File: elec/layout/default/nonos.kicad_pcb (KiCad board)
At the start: 4 copper layers, 45 x 122 mm, 74 parts, among them CN1 HRSHirose_DF40C_100DS_0_4V51, CN2 HRSHirose_DF40C_100DS_0_4V51, Q1 MOSFET, U1 STUSB4500QTR, U2 _Texas_Instruments_SN74LVC1G0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, U3 _Texas_Instruments_TAS5825MRH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, U4 _HCTL_HC_TYPE_C_24P_VS9_3_5A_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, U5 JST_Sales_America_B02B_XASK_1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, U6 JST_Sales_America_B02B_XASK_1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, U7 _Texas_Instruments_TPS56637RP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

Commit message: Update to newest atopile syntax
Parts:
- C11, C12, C7, C8: footprint lcsc:C0603 -> lcsc:CAP-SMD_L1.6-W0.8-3
- C15: value 4.7µF ±10% 16V X5R -> 100nF ±10% 50V X7R
- C16, C20, C21, C22, C27: value 100nF ±10% 16V X7R -> 100nF ±10% 50V X7R; footprint lcsc:C0402 -> lcsc:C0603
- C17, C18, C19: value 22µF ±20% 25V X5R -> 100nF ±10% 50V X7R; footprint lcsc:C0805 -> lcsc:C0603
- C2, C23, C3, C5, C6: value 1µF ±10% 25V X5R -> 1µF ±10% 10V X5R
- C24, C25, C26: value 4.7µF ±10% 25V X5R -> 100nF ±10% 50V X7R; footprint lcsc:C0805 -> lcsc:C0603
- C28: value 47µF ±20% 6.3V X5R -> 100nF ±10% 50V X7R; footprint lcsc:C0805 -> lcsc:C0603
- D4, D5: footprint lcsc:LED0805-R-RD -> lcsc:LED0402-RD
- R13, R14: value 10kΩ ±1% 62.5mW -> 4.7kΩ ±1% 62.5mW
- R15: value 22kΩ ±1% 62.5mW -> 20kΩ ±1% 62.5mW
- R16: value 8.2kΩ ±1% 62.5mW -> 10kΩ ±1% 62.5mW
- R17: value 68kΩ ±1% 62.5mW -> 75kΩ ±1% 62.5mW
- R19, R20: value 5.1kΩ ±1% 62.5mW -> 1kΩ ±1% 100mW; footprint lcsc:R0402 -> lcsc:R0603
- R2, R3: value 4.7kΩ ±1% 62.5mW -> 10kΩ ±1% 62.5mW
- R8, R9: value 470Ω ±1% 62.5mW -> 470Ω ±1% 100mW; footprint lcsc:R0402 -> lcsc:R0603
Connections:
- net pins[26] renamed processor.hdi_b-pins[26]
- net pins[38] renamed processor.hdi_b-pins[38]
- net processor-pins[44]-1 renamed pins[44]
- net processor-pins[46]-1 renamed pins[46]
- net processor.hdi_b-pins[40] renamed pins[40]
- C11 pad 1: amplifier-net-3 -> amplifier-net-8
- C11 pad 2: amplifier-net-2 -> amplifier-net-9
- C12 pad 1: amplifier-net-7 -> amplifier-net-10
- C12 pad 2: amplifier-net -> amplifier-net-11
- C13 pad 1: net-1 -> net-4
- C14 pad 1: net -> net-5
- C23 pad 1: amplifier-net-6 -> amplifier-net
- C29 pad 1: regulator-net -> regulator-net-3
- C29 pad 2: regulator-net-1 -> regulator-net-2
- C30 pad 1: regulator-net-2 -> regulator-net-4
- C30 pad 2: regulator-net-3 -> regulator-net
- C4 pad 1: pd_controller-net-3 -> pd_controller-net-4
- C5 pad 1: amplifier-net-10 -> amplifier-net-5
- C6 pad 1: amplifier-net-1 -> amplifier-net-6
- C7 pad 1: amplifier-net-11 -> amplifier-net-3
- C7 pad 2: amplifier-net-8 -> amplifier-net-4
- C8 pad 1: amplifier-net-4 -> amplifier-net-7
- C8 pad 2: amplifier-net-5 -> amplifier-net-2
- C9 pad 1: net-3 -> net-1
- CN1 pad 12: processor-signal -> processor-signal-1
- CN1 pad 15: signal-3 -> signal-1
- CN1 pad 17: signal-4 -> signal-2
- CN1 pad 24: processor-signal-2 -> processor-signal-5
- CN1 pad 27: signal-5 -> signal-3
- CN1 pad 28: signal-2 -> net
- CN1 pad 29: signal-1 -> net-3
- CN1 pad 77: processor-pins[46] -> processor-signal-6
- CN1 pad 78: processor-pins[44] -> processor-signal-2
- CN1 pad 80: processor-pins[40] -> processor-signal-4
- CN1 pad 81: processor-signal-1 -> processor-pins[38]
- CN1 pad 82: signal -> signal-4
- CN1 pad 85: processor-signal-6 -> pins[30]
- CN1 pad 86: processor-signal-5 -> processor-signal
- CN1 pad 87: processor-signal-4 -> processor-pins[26]
- D4 pad 1: VCC_3V3 -> processor-net-3
- D4 pad 2: processor-net-3 -> VCC_3V3
- D5 pad 1: VCC_3V3 -> processor-net-1
- D5 pad 2: processor-net-1 -> VCC_3V3
- FPC1 pad 10: signal -> signal-4
- FPC1 pad 7: signal-5 -> signal-3
- FPC1 pad 8: signal-4 -> signal-2
- FPC1 pad 9: signal-3 -> signal-1
- L1 pad 1: amplifier-net-8 -> amplifier-net-4
- L1 pad 2: net-3 -> net-1
- L2 pad 1: amplifier-net-5 -> amplifier-net-2
- L3 pad 1: amplifier-net-2 -> amplifier-net-9
- L3 pad 2: net-1 -> net-4
- L4 pad 1: amplifier-net -> amplifier-net-11
- L4 pad 2: net -> net-5
- L5 pad 2: regulator-net-1 -> regulator-net-2
- Q1 pad 4: pd_controller-net-2 -> pd_controller-net
- R1 pad 2: pd_controller-net-1 -> pd_controller-net-3
- R10 pad 1: amplifier-net-9 -> amplifier-net-1
- R11 pad 1: signal-1 -> net
- R12 pad 1: signal-7 -> signal-5
- R13 pad 1: signal-2 -> SCL
- R14 pad 1: signal-6 -> SDA
- R15 pad 2: regulator-net-2 -> regulator-net-4
- R16 pad 2: regulator-net-3 -> regulator-net
- R17 pad 2: regulator-net-3 -> regulator-net
- R18 pad 2: regulator-net-4 -> regulator-net-1
- R2 pad 1: SCL -> net-3
- R3 pad 1: SDA -> signal
- R4 pad 2: pd_controller-net -> pd_controller-net-2
- R5 pad 1: pd_controller-net-2 -> pd_controller-net
- R6 pad 1: pd_controller-net-2 -> pd_controller-net
- R6 pad 2: pd_controller-net-4 -> pd_controller-net-1
- R7 pad 1: pd_controller-net-2 -> pd_controller-net
- R7 pad 2: pd_controller-net-3 -> pd_controller-net-4
- R8 pad 2: rj45-net-1 -> rj45-net
- R9 pad 2: rj45-net -> rj45-net-1
- RJ1 pad 12: rj45-net-1 -> rj45-net
- RJ1 pad 13: rj45-net -> rj45-net-1
- U1 pad 1: pd_controller.pd_controller-signal-1 -> pd_controller.pd_controller-signal
- U1 pad 16: pd_controller-net-4 -> pd_controller-net-1
- U1 pad 18: pd_controller-net -> pd_controller-net-2
- U1 pad 5: pd_controller.pd_controller-signal -> pd_controller.pd_controller-signal-1
- U1 pad 9: pd_controller-net-1 -> pd_controller-net-3
- U3 pad 1: amplifier-net-4 -> amplifier-net-7
- U3 pad 10: signal-7 -> signal
- U3 pad 11: signal-6 -> signal-5
- U3 pad 17: signal-2 -> net
- U3 pad 18: amplifier-net-1 -> amplifier-net-6
- U3 pad 19: amplifier-net-10 -> amplifier-net-5
- U3 pad 2: amplifier-net-5 -> amplifier-net-2
- U3 pad 23: amplifier-net -> amplifier-net-11
- U3 pad 24: amplifier-net-7 -> amplifier-net-10
- U3 pad 27: amplifier-net-2 -> amplifier-net-9
- U3 pad 28: amplifier-net-3 -> amplifier-net-8
- U3 pad 29: amplifier-net-11 -> amplifier-net-3
- U3 pad 30: amplifier-net-8 -> amplifier-net-4
- U3 pad 7: amplifier-net-6 -> amplifier-net
- U3 pad 8: amplifier-net-9 -> amplifier-net-1
- U3 pad 9: signal-1 -> net-3
- U5 pad 2: net-3 -> net-1
- U6 pad 1: net-1 -> net-4
- U6 pad 2: net -> net-5
- U7 pad 2: regulator-net-3 -> regulator-net
- U7 pad 4: regulator-net-4 -> regulator-net-1
- U7 pad 6: regulator-net-1 -> regulator-net-2
- U7 pad 7: regulator-net -> regulator-net-3
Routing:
- net (no net): track 0.00 -> 3.61 mm
- net signal-7: track 1.91 -> 0.00 mm
- net signal-6: track 1.70 -> 0.00 mm

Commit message: Build full
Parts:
- D2, D3: value (none) -> infV
- D4, D5: value (none) -> 2V; footprint lcsc:LED0402-RD -> lcsc:LED0603-RD
- L1, L2, L3, L4: value 10µH ±20% 4.5A 68mΩ -> 10µH ±20% infHz 4.5A 68mΩ
- L5: value 3.3µH ±20% 4A 73mΩ -> 3.3µH ±20% infHz 4A 73mΩ
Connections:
- net pins[28] renamed processor.hdi_b-pins[28]
- net processor-pins[26] renamed processor-signal-8
- net processor.hdi_b-pins[26] renamed pins[26]
- net processor.hdi_b-pins[38] renamed pins[38]
- net processor.hdi_b-pins[39] renamed pins[39]
- C10 pad 1: net-2 -> net-3
- C11 pad 1: amplifier-net-8 -> amplifier-net-1
- C11 pad 2: amplifier-net-9 -> amplifier-net-2
- C12 pad 1: amplifier-net-10 -> amplifier-net-8
- C12 pad 2: amplifier-net-11 -> amplifier-net
- C14 pad 1: net-5 -> net
- C23 pad 1: amplifier-net -> amplifier-net-4
- C29 pad 1: regulator-net-3 -> regulator-net-4
- C29 pad 2: regulator-net-2 -> regulator-net-3
- C30 pad 1: regulator-net-4 -> regulator-net-1
- C5 pad 1: amplifier-net-5 -> amplifier-net-10
- C6 pad 1: amplifier-net-6 -> amplifier-net-9
- C7 pad 1: amplifier-net-3 -> amplifier-net-6
- C7 pad 2: amplifier-net-4 -> amplifier-net-3
- C8 pad 2: amplifier-net-2 -> amplifier-net-11
- C9 pad 1: net-1 -> net-5
- CN1 pad 12: processor-signal-1 -> processor-signal-7
- CN1 pad 15: signal-1 -> signal-4
- CN1 pad 20: processor-pins[39] -> processor-signal-5
- CN1 pad 22: processor-signal-3 -> processor-signal
- CN1 pad 23: pins[45] -> processor-signal-2
- CN1 pad 24: processor-signal-5 -> pins[47]
- CN1 pad 28: net -> net-1
- CN1 pad 29: net-3 -> net-2
- CN1 pad 75: pins[50] -> processor-signal-1
- CN1 pad 77: processor-signal-6 -> processor-signal-9
- CN1 pad 78: processor-signal-2 -> processor-signal-4
- CN1 pad 80: processor-signal-4 -> processor-signal-3
- CN1 pad 81: processor-pins[38] -> processor-signal-6
- CN1 pad 82: signal-4 -> signal-5
- CN1 pad 86: processor-signal -> processor-pins[28]
- D5 pad 1: processor-net-1 -> processor-net
- FPC1 pad 10: signal-4 -> signal-5
- FPC1 pad 9: signal-1 -> signal-4
- L1 pad 1: amplifier-net-4 -> amplifier-net-3
- L1 pad 2: net-1 -> net-5
- L2 pad 1: amplifier-net-2 -> amplifier-net-11
- L2 pad 2: net-2 -> net-3
- L3 pad 1: amplifier-net-9 -> amplifier-net-2
- L4 pad 1: amplifier-net-11 -> amplifier-net
- L4 pad 2: net-5 -> net
- L5 pad 2: regulator-net-2 -> regulator-net-3
- R1 pad 2: pd_controller-net-3 -> pd_controller-net-1
- R10 pad 1: amplifier-net-1 -> amplifier-net-5
- R11 pad 1: net -> net-1
- R12 pad 1: signal-5 -> signal-1
- R15 pad 2: regulator-net-4 -> regulator-net-1
- R18 pad 2: regulator-net-1 -> regulator-net-2
- R2 pad 1: net-3 -> net-2
- R20 pad 1: processor-net-1 -> processor-net
- R20 pad 2: processor-net -> processor-net-1
- R4 pad 2: pd_controller-net-2 -> pd_controller-net-3
- R6 pad 2: pd_controller-net-1 -> pd_controller-net-2
- R8 pad 2: rj45-net -> rj45-net-1
- R9 pad 2: rj45-net-1 -> rj45-net
- RJ1 pad 12: rj45-net -> rj45-net-1
- RJ1 pad 13: rj45-net-1 -> rj45-net
- U1 pad 1: pd_controller.pd_controller-signal -> pd_controller.pd_controller-signal-1
- U1 pad 16: pd_controller-net-1 -> pd_controller-net-2
- U1 pad 18: pd_controller-net-2 -> pd_controller-net-3
- U1 pad 5: pd_controller.pd_controller-signal-1 -> pd_controller.pd_controller-signal
- U1 pad 9: pd_controller-net-3 -> pd_controller-net-1
- U2 pad 4: processor-net -> processor-net-1
- U3 pad 11: signal-5 -> signal-1
- U3 pad 17: net -> net-1
- U3 pad 18: amplifier-net-6 -> amplifier-net-9
- U3 pad 19: amplifier-net-5 -> amplifier-net-10
- U3 pad 2: amplifier-net-2 -> amplifier-net-11
- U3 pad 23: amplifier-net-11 -> amplifier-net
- U3 pad 24: amplifier-net-10 -> amplifier-net-8
- U3 pad 27: amplifier-net-9 -> amplifier-net-2
- U3 pad 28: amplifier-net-8 -> amplifier-net-1
- U3 pad 29: amplifier-net-3 -> amplifier-net-6
- U3 pad 30: amplifier-net-4 -> amplifier-net-3
- U3 pad 7: amplifier-net -> amplifier-net-4
- U3 pad 8: amplifier-net-1 -> amplifier-net-5
- U3 pad 9: net-3 -> net-2
- U5 pad 1: net-2 -> net-3
- U5 pad 2: net-1 -> net-5
- U6 pad 2: net-5 -> net
- U7 pad 4: regulator-net-1 -> regulator-net-2
- U7 pad 6: regulator-net-2 -> regulator-net-3
- U7 pad 7: regulator-net-3 -> regulator-net-4

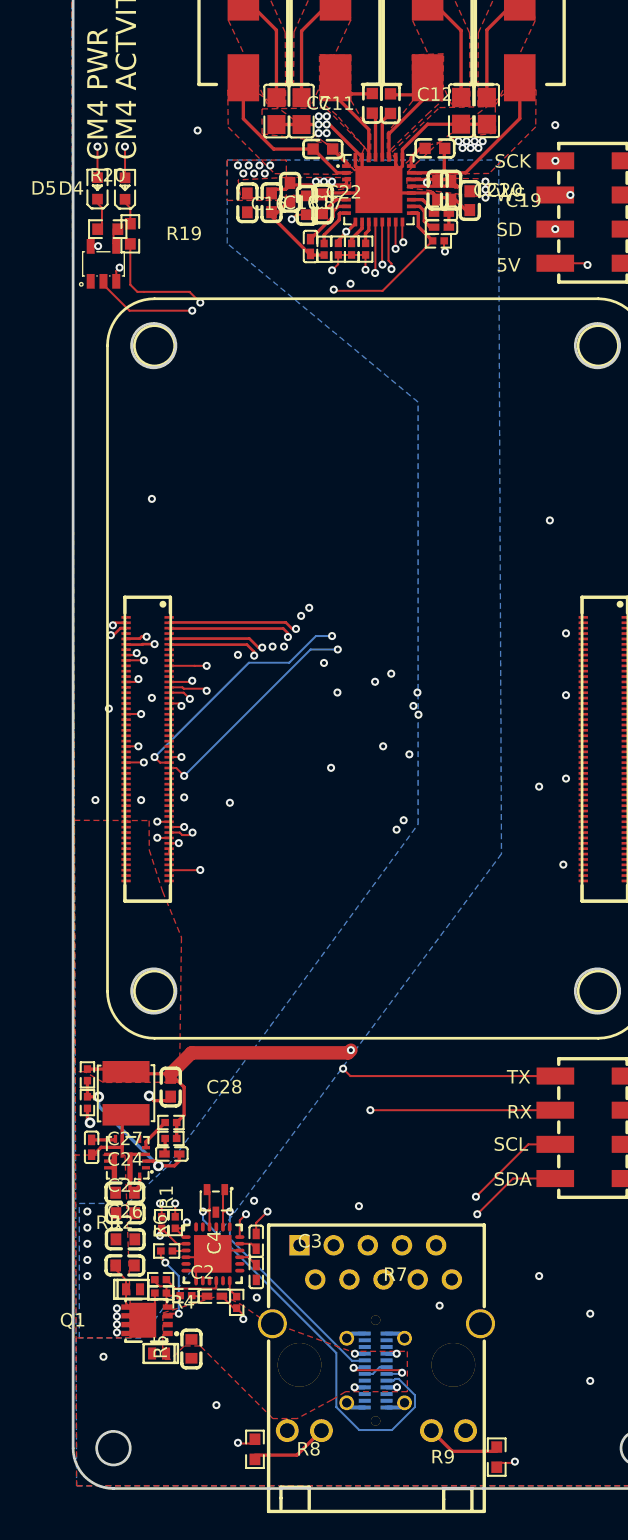
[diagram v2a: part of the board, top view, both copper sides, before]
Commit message: Don't update PCB files
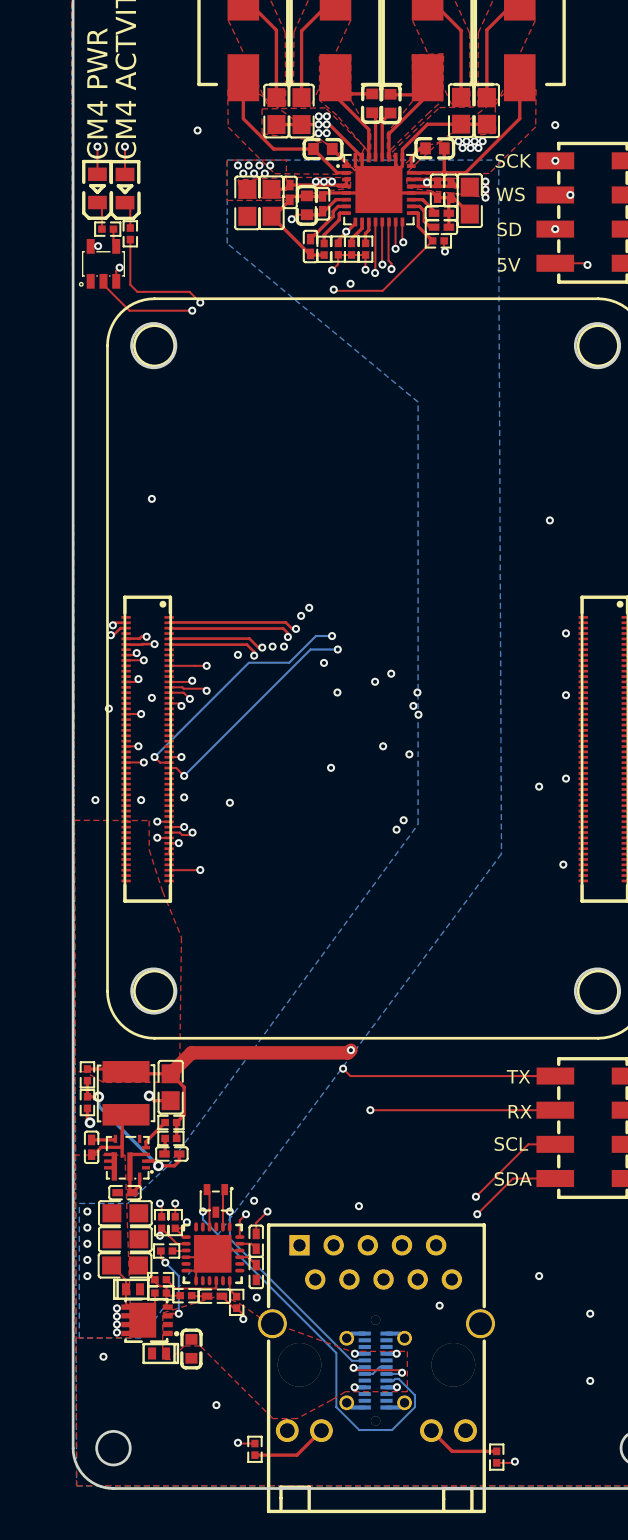
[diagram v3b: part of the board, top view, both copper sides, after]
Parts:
- C11, C12, C7, C8: footprint lcsc:CAP-SMD_L1.6-W0.8-3 -> lcsc:C0603
- C15: value 100nF ±10% 50V X7R -> 4.7µF ±10% 16V X5R
- C16, C20, C21, C22, C27: value 100nF ±10% 50V X7R -> 100nF ±10% 16V X7R; footprint lcsc:C0603 -> lcsc:C0402
- C17, C18, C19: value 100nF ±10% 50V X7R -> 22µF ±20% 25V X5R; footprint lcsc:C0603 -> lcsc:C0805
- C2, C23, C3, C5, C6: value 1µF ±10% 10V X5R -> 1µF ±10% 25V X5R
- C24, C25, C26: value 100nF ±10% 50V X7R -> 4.7µF ±10% 25V X5R; footprint lcsc:C0603 -> lcsc:C0805
- C28: value 100nF ±10% 50V X7R -> 47µF ±20% 6.3V X5R; footprint lcsc:C0603 -> lcsc:C0805
- D2, D3: value infV -> (none)
- D4, D5: value 2V -> (none); footprint lcsc:LED0603-RD -> lcsc:LED0805-R-RD
- L1, L2, L3, L4: value 10µH ±20% infHz 4.5A 68mΩ -> 10µH ±20% 4.5A 68mΩ
- L5: value 3.3µH ±20% infHz 4A 73mΩ -> 3.3µH ±20% 4A 73mΩ
- R13, R14: value 4.7kΩ ±1% 62.5mW -> 10kΩ ±1% 62.5mW
- R15: value 20kΩ ±1% 62.5mW -> 22kΩ ±1% 62.5mW
- R16: value 10kΩ ±1% 62.5mW -> 8.2kΩ ±1% 62.5mW
- R17: value 75kΩ ±1% 62.5mW -> 68kΩ ±1% 62.5mW
- R19, R20: value 1kΩ ±1% 100mW -> 5.1kΩ ±1% 62.5mW; footprint lcsc:R0603 -> lcsc:R0402
- R2, R3: value 10kΩ ±1% 62.5mW -> 4.7kΩ ±1% 62.5mW
- R8, R9: value 470Ω ±1% 100mW -> 470Ω ±1% 62.5mW; footprint lcsc:R0603 -> lcsc:R0402
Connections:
- net pins[39] renamed processor.hdi_b-pins[39]
- net pins[40] renamed processor.hdi_b-pins[40]
- net pins[44] renamed processor-pins[44]-1
- net pins[46] renamed processor-pins[46]-1
- net processor-signal-9 renamed processor-pins[46]
- net processor.hdi_b-pins[28] renamed pins[28]
- C10 pad 1: net-3 -> net-2
- C11 pad 1: amplifier-net-1 -> amplifier-net-3
- C12 pad 1: amplifier-net-8 -> amplifier-net-7
- C13 pad 1: net-4 -> net-1
- C23 pad 1: amplifier-net-4 -> amplifier-net-6
- C29 pad 1: regulator-net-4 -> regulator-net
- C29 pad 2: regulator-net-3 -> regulator-net-1
- C30 pad 1: regulator-net-1 -> regulator-net-2
- C30 pad 2: regulator-net -> regulator-net-3
- C4 pad 1: pd_controller-net-4 -> pd_controller-net-3
- C6 pad 1: amplifier-net-9 -> amplifier-net-1
- C7 pad 1: amplifier-net-6 -> amplifier-net-11
- C7 pad 2: amplifier-net-3 -> amplifier-net-8
- C8 pad 1: amplifier-net-7 -> amplifier-net-4
- C8 pad 2: amplifier-net-11 -> amplifier-net-5
- C9 pad 1: net-5 -> net-3
- CN1 pad 12: processor-signal-7 -> processor-signal
- CN1 pad 15: signal-4 -> signal-3
- CN1 pad 17: signal-2 -> signal-4
- CN1 pad 20: processor-signal-5 -> processor-pins[39]
- CN1 pad 22: processor-signal -> processor-signal-3
- CN1 pad 23: processor-signal-2 -> pins[45]
- CN1 pad 24: pins[47] -> processor-signal-2
- CN1 pad 27: signal-3 -> signal-5
- CN1 pad 28: net-1 -> signal-2
- CN1 pad 29: net-2 -> signal-1
- CN1 pad 75: processor-signal-1 -> pins[50]
- CN1 pad 78: processor-signal-4 -> processor-pins[44]
- CN1 pad 80: processor-signal-3 -> processor-pins[40]
- CN1 pad 81: processor-signal-6 -> processor-signal-1
- CN1 pad 82: signal-5 -> signal
- CN1 pad 85: pins[30] -> processor-signal-6
- CN1 pad 86: processor-pins[28] -> processor-signal-5
- CN1 pad 87: processor-signal-8 -> processor-signal-4
- D4 pad 1: processor-net-3 -> VCC_3V3
- D4 pad 2: VCC_3V3 -> processor-net-3
- D5 pad 1: processor-net -> VCC_3V3
- D5 pad 2: VCC_3V3 -> processor-net-1
- FPC1 pad 10: signal-5 -> signal
- FPC1 pad 7: signal-3 -> signal-5
- FPC1 pad 8: signal-2 -> signal-4
- FPC1 pad 9: signal-4 -> signal-3
- L1 pad 1: amplifier-net-3 -> amplifier-net-8
- L1 pad 2: net-5 -> net-3
- L2 pad 1: amplifier-net-11 -> amplifier-net-5
- L2 pad 2: net-3 -> net-2
- L3 pad 2: net-4 -> net-1
- L5 pad 2: regulator-net-3 -> regulator-net-1
- Q1 pad 4: pd_controller-net -> pd_controller-net-2
- R10 pad 1: amplifier-net-5 -> amplifier-net-9
- R11 pad 1: net-1 -> signal-1
- R12 pad 1: signal-1 -> signal-7
- R13 pad 1: SCL -> signal-2
- R14 pad 1: SDA -> signal-6
- R15 pad 2: regulator-net-1 -> regulator-net-2
- R16 pad 2: regulator-net -> regulator-net-3
- R17 pad 2: regulator-net -> regulator-net-3
- R18 pad 2: regulator-net-2 -> regulator-net-4
- R2 pad 1: net-2 -> SCL
- R20 pad 1: processor-net -> processor-net-1
- R20 pad 2: processor-net-1 -> processor-net
- R3 pad 1: signal -> SDA
- R4 pad 2: pd_controller-net-3 -> pd_controller-net
- R5 pad 1: pd_controller-net -> pd_controller-net-2
- R6 pad 1: pd_controller-net -> pd_controller-net-2
- R6 pad 2: pd_controller-net-2 -> pd_controller-net-4
- R7 pad 1: pd_controller-net -> pd_controller-net-2
- R7 pad 2: pd_controller-net-4 -> pd_controller-net-3
- U1 pad 16: pd_controller-net-2 -> pd_controller-net-4
- U1 pad 18: pd_controller-net-3 -> pd_controller-net
- U2 pad 4: processor-net-1 -> processor-net
- U3 pad 1: amplifier-net-7 -> amplifier-net-4
- U3 pad 10: signal -> signal-7
- U3 pad 11: signal-1 -> signal-6
- U3 pad 17: net-1 -> signal-2
- U3 pad 18: amplifier-net-9 -> amplifier-net-1
- U3 pad 2: amplifier-net-11 -> amplifier-net-5
- U3 pad 24: amplifier-net-8 -> amplifier-net-7
- U3 pad 28: amplifier-net-1 -> amplifier-net-3
- U3 pad 29: amplifier-net-6 -> amplifier-net-11
- U3 pad 30: amplifier-net-3 -> amplifier-net-8
- U3 pad 7: amplifier-net-4 -> amplifier-net-6
- U3 pad 8: amplifier-net-5 -> amplifier-net-9
- U3 pad 9: net-2 -> signal-1
- U5 pad 1: net-3 -> net-2
- U5 pad 2: net-5 -> net-3
- U6 pad 1: net-4 -> net-1
- U7 pad 2: regulator-net -> regulator-net-3
- U7 pad 4: regulator-net-2 -> regulator-net-4
- U7 pad 6: regulator-net-3 -> regulator-net-1
- U7 pad 7: regulator-net-4 -> regulator-net
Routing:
- net (no net): track 3.61 -> 0.00 mm
- net signal-7: track 0.00 -> 1.91 mm
- net signal-6: track 0.00 -> 1.70 mm
